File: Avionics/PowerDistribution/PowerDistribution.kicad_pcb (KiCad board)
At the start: 4 copper layers, 90.2 x 96 mm, 165 parts, among them J1 Conn_02x26_Odd_Even, J10 Conn_01x02, J11 Conn_01x04, J12 Conn_01x04, J13 Conn_01x04, J14 Conn_01x02, J15 Conn_01x02, J2 Conn_02x26_Odd_Even, J3 Conn_01x02, J4 Conn_01x02, J5 Conn_01x02, J6 Conn_01x02, J7 USB_C_Receptacle_USB2.0_14P, J8 Conn_01x02, J9 Conn_01x02, Q1 BC848ALT1G, Q2 IRLML2803PBFCT, Q3 IRLML2803PBFCT, U1 LT8610, U16 INA219AxD, U17 INA219AxD, U18 INA219AxD, U19 LT3652EDD, U2 LT8610, U21 INA219AxD, U6 LT8610

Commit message: PDU 3.0.0
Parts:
- added TP1: ~, TestPoint:TestPoint_Pad_2.0x2.0mm, F.Cu at (132.5, 53.5)
- added TP2: ~, TestPoint:TestPoint_Pad_2.0x2.0mm, F.Cu at (132.5, 57.5)
- added TP3: ~, TestPoint:TestPoint_Pad_2.0x2.0mm, F.Cu at (132.5, 61.6)
- added TP4: ~, TestPoint:TestPoint_Pad_2.0x2.0mm, F.Cu at (132.5, 65.6)
- added TP5: ~, TestPoint:TestPoint_Pad_2.0x2.0mm, F.Cu at (136.5, 53.5)
- added TP6: ~, TestPoint:TestPoint_Pad_2.0x2.0mm, F.Cu at (136.5, 57.5)
- added TP7: ~, TestPoint:TestPoint_Pad_2.0x2.0mm, F.Cu at (136.5, 61.6)
- moved C22 62.9 mm to (267.3, 75.2)
- moved U6 62.9 mm to (273.1, 73.7)
- moved C19 62.9 mm to (278.2, 71.9)
- moved C20 62.9 mm to (276.9, 74.9)
- moved C21 62.9 mm to (266.7, 69.1)
- moved C23 62.9 mm to (265.2, 73.4)
- moved C24 62.9 mm to (274.0, 77.9)
- moved L3 62.9 mm to (270.7, 78.4)
- moved R10 62.9 mm to (266.7, 71.1)
- moved R7 62.9 mm to (278.2, 72.9)
- moved R9 62.9 mm to (270.9, 69.3)
- moved R29 53.6 mm to (143.7, 95.3)
- moved C49 53.6 mm to (145.2, 93.8)
- moved C28 53.6 mm to (153.7, 93.8)
- moved R42 53.6 mm to (143.8, 102.1)
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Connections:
- net /BURN_FET renamed BURN_FET
- net /EDFA_5V renamed EDFA_5V
- net /EDFA_5V_STAT renamed EDFA_5V_STAT
- net /ENAB_BURN_1 renamed ENAB_BURN_1
- net /ENAB_BURN_2 renamed ENAB_BURN_2
- net /KAPTON_PWR renamed KAPTON_PWR
- net /SCL renamed SCL
- net /SDA renamed SDA
- net /SOLAR_PRE_INH renamed SOLAR_PRE_INH
- C12 pad 2: /3V3_BUS -> 3V3
- C14 pad 1: /EDFA_5V_SW -> EDFA_5V_S
- C17 pad 1: /5V_BUS -> 5V
- C20 pad 1: GNDA -> V_BATT
- C20 pad 2: V_BATT -> GNDA
- C21 pad 2: /5V_BUS -> 5V
- C24 pad 2: /5V_BUS -> 5V
- C25 pad 1: /5V_BUS -> 5V
- C26 pad 1: /5V_SW_1 -> 5V_S
- C29 pad 1: /3V3_BUS -> 3V3
- C30 pad 1: /PERIPH_PWR -> 3V3_S
- C45 pad 2: /PERIPH_PWR -> 3V3_S
- C46 pad 2: /PERIPH_PWR -> 3V3_S
- C47 pad 2: /PERIPH_PWR -> 3V3_S
- C50 pad 2: /PERIPH_PWR -> 3V3_S
- C9 pad 2: /3V3_BUS -> 3V3
- D1 pad 2: /5V_BUS -> 5V
- D13 pad 2: /PERIPH_PWR -> 3V3_S
- D3 pad 2: /3V3_BUS -> 3V3
- D4 pad 2: /EDFA_5V_SW -> EDFA_5V_S
- D6 pad 2: /5V_SW_1 -> 5V_S
- J1 pad 10: unconnected-(J1-Pin_10-Pad10) -> GND_REF
- J1 pad 11: /KAPTON_ENABLE -> GND_REF
- J1 pad 12: unconnected-(J1-Pin_12-Pad12) -> GND_REF
- J1 pad 13: /EDFA_ENABLE -> /KAPTON_ENABLE
- J1 pad 15: unconnected-(J1-Pin_15-Pad15) -> /EDFA_ENABLE
- J1 pad 9: unconnected-(J1-Pin_9-Pad9) -> GND_REF
- J2 pad 1: /SOLAR_TMP_4 -> unconnected-(J2-Pin_1-Pad1)
- J2 pad 2: /SOLAR_TMP_5 -> /PDU_TEMP
- J2 pad 45: unconnected-(J2-Pin_45-Pad45) -> V_BATT
- L2 pad 2: /3V3_BUS -> 3V3
- L3 pad 2: /5V_BUS -> 5V
- R10 pad 2: /5V_BUS -> 5V
- R57 pad 1: V_BATT -> /BATT_CS
- R58 pad 1: /BATT_CS -> V_BATT
- R58 pad 2: V_BATT -> /BATT_CS
- R59 pad 1: /BATT_CS -> V_BATT
- R8 pad 2: /3V3_BUS -> 3V3
- U10 pad 1: /5V_SW_1 -> 5V_S
- U10 pad 2: /5V_BUS -> 5V
- U10 pad 3: /5V_BUS -> 5V
- U10 pad 4: /5V_SW_1_EN -> 5V_S_EN
- U10 pad 6: /5V_BUS -> 5V
- U10 pad 7: /5V_BUS -> 5V
- U10 pad 8: /5V_SW_1 -> 5V_S
- U14 pad 1: /PERIPH_PWR -> 3V3_S
- U14 pad 2: /3V3_BUS -> 3V3
- U14 pad 3: /3V3_BUS -> 3V3
- U14 pad 4: /PERIPH_EN -> 3V3_S_EN
- U14 pad 6: /3V3_BUS -> 3V3
- U14 pad 7: /3V3_BUS -> 3V3
- U14 pad 8: /PERIPH_PWR -> 3V3_S
- U16 pad 5: /PERIPH_PWR -> 3V3_S
- U17 pad 5: /PERIPH_PWR -> 3V3_S
- U18 pad 5: /PERIPH_PWR -> 3V3_S
- U19 pad 4: /CHRG -> /~{CHRG}
- U19 pad 5: /FAULT -> /~{FAULT}
- U2 pad 14: /3V3_BUS -> 3V3
- U2 pad 15: /3V3_BUS_STAT -> 3V3_STAT
- U21 pad 5: /PERIPH_PWR -> 3V3_S
- U3 pad 1: /EDFA_5V_SW -> EDFA_5V_S
- U3 pad 4: /EDFA_ENABLE -> EDFA_5V_EN
- U3 pad 8: /EDFA_5V_SW -> EDFA_5V_S
- U6 pad 14: /5V_BUS -> 5V
- U6 pad 15: /5V_BUS_STAT -> 5V_STAT
- U9 pad 2: /5V_BUS -> 5V
- U9 pad 3: /5V_BUS -> 5V
- U9 pad 4: /KAPTON_ENABLE -> KAPTON_EN
- U9 pad 6: /5V_BUS -> 5V
- U9 pad 7: /5V_BUS -> 5V
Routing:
- net 3V3_S: track 0.00 -> 124.8 mm, vias 0 -> 5
- net /PERIPH_PWR: track 141.5 -> 16.7 mm, vias 5 -> 0
- net 5V: track 0.00 -> 115.8 mm, vias 0 -> 9
- net /5V_BUS: track 148.9 -> 33.1 mm, vias 9 -> 0
- net (no net): track 0.00 -> 88.5 mm, vias 0 -> 2
- net 5V_S: track 0.00 -> 70.9 mm, vias 0 -> 2
- net /5V_SW_1: track 70.9 -> 0.00 mm, vias 2 -> 0
- net 5V_S_EN: track 0.00 -> 68.1 mm, vias 0 -> 1
- net /5V_SW_1_EN: track 68.1 -> 0.00 mm, vias 1 -> 0
- net EDFA_5V_EN: track 0.00 -> 62.1 mm, vias 0 -> 1
- net /EDFA_ENABLE: track 62.1 -> 0.00 mm, vias 1 -> 0
- net 3V3_S_EN: track 0.00 -> 57.2 mm, vias 0 -> 1
- net /PERIPH_EN: track 57.2 -> 0.00 mm, vias 1 -> 0
- net EDFA_5V_STAT: track 60.9 -> 4.07 mm
- net 3V3: track 0.00 -> 50.9 mm, vias 0 -> 4
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- removed copper zone on B.Cu, net GND
- removed copper zone on F.Cu, net GND
- removed copper zone on In1.Cu, net GND
- removed copper zone on In2.Cu, net V_BATT

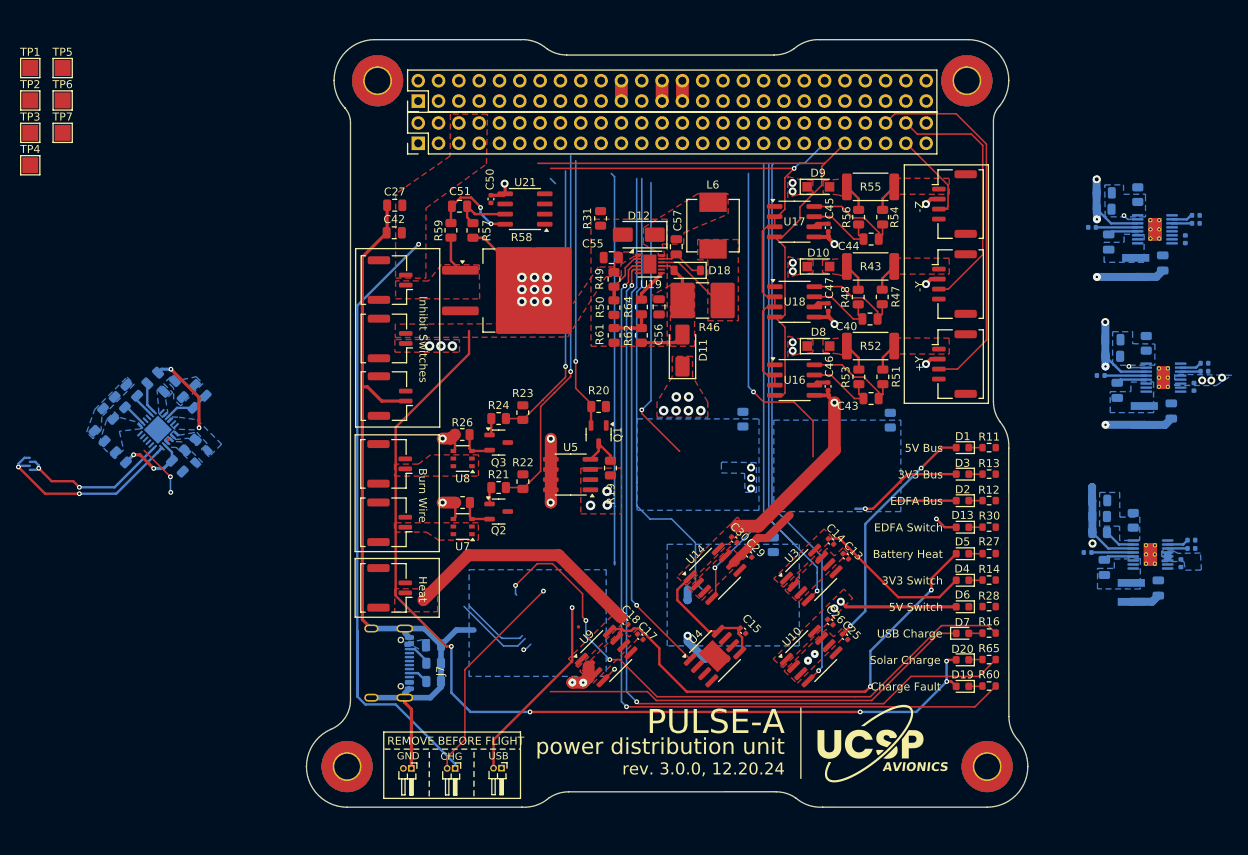
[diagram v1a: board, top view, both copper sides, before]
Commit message: feat: Batt Board v2, PDU v3 in progress; refactor: various cleanups
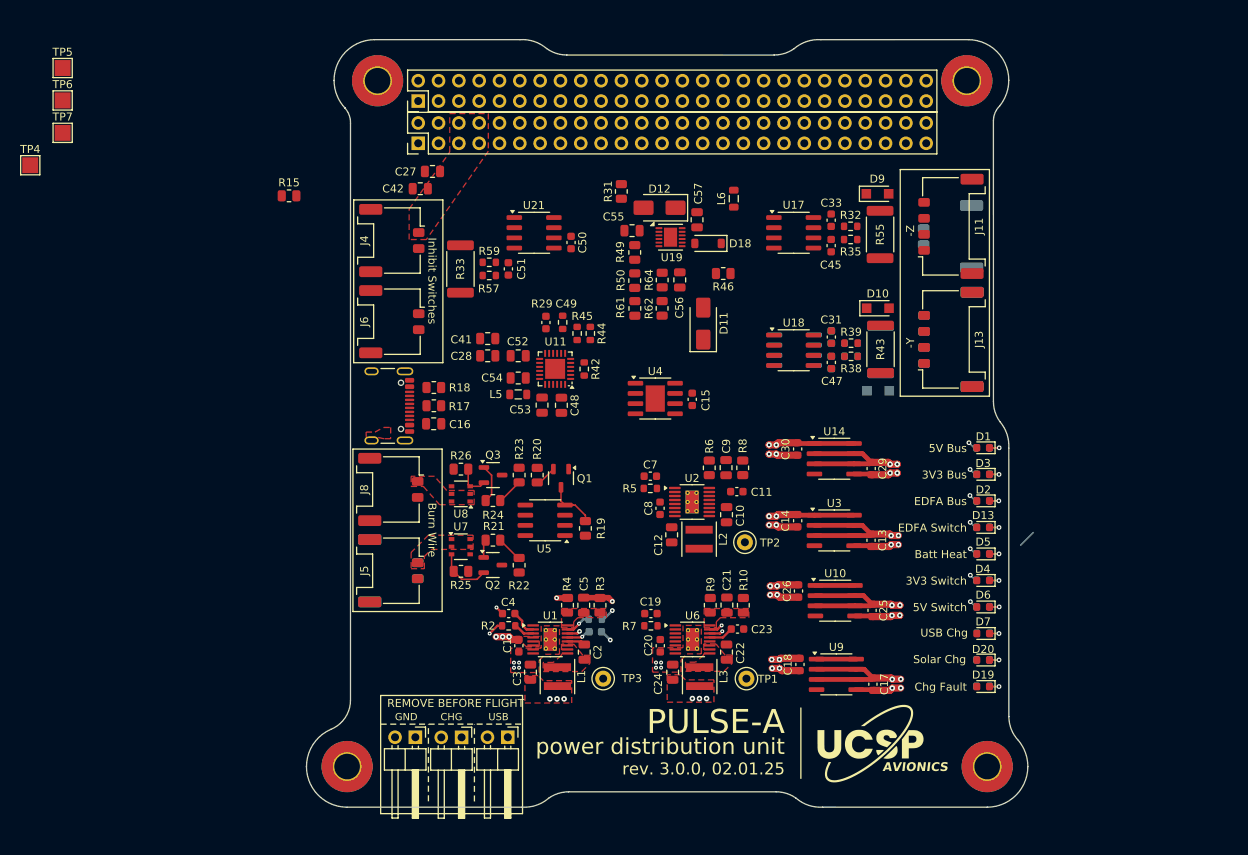
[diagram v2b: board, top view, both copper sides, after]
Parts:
- removed C40, C43, C44: 1uF, Capacitor_SMD:C_0805_2012Metric
- removed R34: 0, Resistor_SMD:R_0805_2012Metric
- removed R47, R48, R51, R53, R54, R56: 10, Resistor_SMD:R_0805_2012Metric
- removed R58: 2m, Package_TO_SOT_SMD:TO-263-2
- added C31: 1uF, Capacitor_SMD:C_0603_1608Metric, F.Cu at (232.6, 87.1)
- added C32: 1uF, Capacitor_SMD:C_0603_1608Metric, B.Cu at (232.6, 90.3)
- added C33: 1uF, Capacitor_SMD:C_0603_1608Metric, F.Cu at (232.6, 72.5)
- added R32: 10, Resistor_SMD:R_0603_1608Metric, F.Cu at (235.0, 73.3)
- added R35: 10, Resistor_SMD:R_0603_1608Metric, F.Cu at (235.0, 74.9)
- added R36: 10, Resistor_SMD:R_0603_1608Metric, B.Cu at (235.1, 87.9)
- added R37: 10, Resistor_SMD:R_0603_1608Metric, B.Cu at (235.1, 89.5)
- added R38: 10, Resistor_SMD:R_0603_1608Metric, F.Cu at (235.1, 89.5)
- added R39: 10, Resistor_SMD:R_0603_1608Metric, F.Cu at (235.1, 87.9)
- C1, C11, C19, C20, C23, C4, C7, C8: footprint Capacitor_SMD:C_0402_1005Metric -> Capacitor_SMD:C_0603_1608Metric; moved to F.Cu
- C10, C12, C16, C2, C21, C22, C24, C28, C3, C41, C48, C5, C52, C53, C54, C9, J7, L1, L2, L3, L5, R10, R15, R17, R18, R3, R4, R6, R8, R9, U1, U11, U2, U6: moved to F.Cu
- C13, C14, C15, C17, C18, C25, C26, C29, C30, C45, C47, C50, C6: footprint Capacitor_SMD:C_0402_1005Metric -> Capacitor_SMD:C_0603_1608Metric
- C46: footprint Capacitor_SMD:C_0402_1005Metric -> Capacitor_SMD:C_0603_1608Metric; moved to B.Cu
- C49: footprint Capacitor_SMD:C_0805_2012Metric -> Capacitor_SMD:C_0603_1608Metric; moved to F.Cu
- C51: footprint Capacitor_SMD:C_0805_2012Metric -> Capacitor_SMD:C_0603_1608Metric
- D13, D4, D5, D6: value 150060RS75000 -> 150060AS75000
- D8, R11, R12, R13, R14, R16, R27, R28, R52, R60, R65, U16: moved to B.Cu
- J10, J14, J9: footprint Connector_PinHeader_1.00mm:PinHeader_1x02_P1.00mm_Horizontal -> Connector_PinHeader_2.54mm:PinHeader_1x02_P2.54mm_Horizontal
- J11, J13: footprint Connector_Molex:Molex_CLIK-Mate_502382-0470_1x04-1MP_P1.25mm_Vertical -> Connector_Molex:Molex_Pico-Lock_205338-0004_1x04-1MP_P2.00mm_Horizontal
- J12: footprint Connector_Molex:Molex_CLIK-Mate_502382-0470_1x04-1MP_P1.25mm_Vertical -> Connector_Molex:Molex_Pico-Lock_205338-0004_1x04-1MP_P2.00mm_Horizontal; moved to B.Cu
- J15, J3: footprint Connector_Molex:Molex_CLIK-Mate_502382-0270_1x02-1MP_P1.25mm_Vertical -> Connector_Molex:Molex_Pico-Lock_205338-0002_1x02-1MP_P2.00mm_Horizontal; moved to B.Cu
- J4, J5, J6, J8: footprint Connector_Molex:Molex_CLIK-Mate_502382-0270_1x02-1MP_P1.25mm_Vertical -> Connector_Molex:Molex_Pico-Lock_205338-0002_1x02-1MP_P2.00mm_Horizontal
- L6: footprint Inductor_SMD:L_Vishay_IHLP-2525 -> Inductor_SMD:L_0805_2012Metric
- R1, R57, R59: footprint Resistor_SMD:R_0805_2012Metric -> Resistor_SMD:R_0603_1608Metric
- R2, R5, R7: footprint Capacitor_SMD:C_0402_1005Metric -> Resistor_SMD:R_0603_1608Metric; moved to F.Cu
- R29, R42, R44, R45: footprint Resistor_SMD:R_0805_2012Metric -> Resistor_SMD:R_0603_1608Metric; moved to F.Cu
- R30: value 150 -> 65; moved to B.Cu
- R33: value 0 -> 2m; footprint Resistor_SMD:R_0805_2012Metric -> Resistor_SMD:R_2512_6332Metric; moved to F.Cu
- R46: footprint Resistor_SMD:R_2816_7142Metric -> Resistor_SMD:R_0805_2012Metric
- TP1, TP2, TP3: footprint TestPoint:TestPoint_Pad_2.0x2.0mm -> TestPoint:TestPoint_Keystone_5000-5004_Miniature
- moved TP1 117.6 mm to (222.0, 129.8)
- moved TP2 105.0 mm to (221.8, 112.8)
- moved TP3 98.9 mm to (204.1, 129.8)
- moved R2 85.9 mm to (192.3, 123.2), turned to 180 degrees
- moved C4 85.8 mm to (192.3, 121.7), turned to 0 degrees
- moved R7 84.7 mm to (210.1, 123.2), turned to 180 degrees
- moved C19 84.4 mm to (210.1, 121.7), turned to 0 degrees
- moved C1 83.4 mm to (193.5, 125.7)
- moved C20 83.0 mm to (211.2, 125.7), turned to -90 degrees
- moved C24 79.8 mm to (212.8, 129.0)
- moved C3 79.2 mm to (195.0, 129.0)
- moved U6 77.2 mm to (215.3, 124.9), turned to 0 degrees
- moved U1 75.8 mm to (197.5, 124.9), turned to 0 degrees
- moved L3 74.7 mm to (216.2, 129.6)
- moved R15 74.6 mm to (164.8, 69.5), turned to 0 degrees
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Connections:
- net /EDFA_ENABLE renamed /EDFA_EN
- C1 pad 1: GNDA -> GND
- C11 pad 2: GNDA -> GND
- C12 pad 1: GNDA -> GND
- C15 pad 2: /PERIPH_PWR -> 3V3
- C19 pad 1: GNDA -> GND
- C20 pad 2: GNDA -> GND
- C23 pad 2: GNDA -> GND
- C24 pad 1: GNDA -> GND
- C27 pad 2: /BATT_PRE_INH -> /BATT_RAW
- C3 pad 1: GNDA -> GND
- C4 pad 1: GNDA -> GND
- C42 pad 2: /BATT_PRE_INH -> /BATT_RAW
- C6 pad 2: GNDA -> GND
- C7 pad 1: GNDA -> GND
- C8 pad 1: GNDA -> GND
- J1 pad 13: /KAPTON_ENABLE -> KAPTON_EN
- J1 pad 21: /5V_SW_1 -> 5V_S
- J1 pad 22: /ICL -> /FAULT
- J1 pad 31: /5V_SW_1_EN -> 5V_S_EN
- J1 pad 5: /BATT_PRE_INH -> /RAW_BATT
- J1 pad 6: /BATT_PRE_INH -> /RAW_BATT
- J1 pad 7: /BATT_PRE_INH -> /RAW_BATT
- J1 pad 8: /BATT_PRE_INH -> /RAW_BATT
- J2 pad 21: /EDFA_5V_SW -> EDFA_5V_S
- J2 pad 22: /EDFA_5V_SW -> EDFA_5V_S
- J2 pad 25: /5V_BUS -> 5V
- J2 pad 26: /5V_BUS -> 5V
- J2 pad 27: /3V3_BUS -> 3V3
- J2 pad 28: /3V3_BUS -> 3V3
- J4 pad 1: /BATT_CS -> /BATT_RAW
- J4 pad 2: /BATT_PRE_INH -> /BATT_CS
- J9 pad 1: /BATT_PRE_INH -> /BATT_RAW
- R2 pad 2: GNDA -> GND
- R33 pad 1: GNDA -> /BATT_CS
- R33 pad 2: GND -> V_BATT
- R4 pad 1: GNDA -> GND
- R5 pad 2: GNDA -> GND
- R6 pad 1: GNDA -> GND
- R7 pad 2: GNDA -> GND
- R9 pad 1: GNDA -> GND
- U1 pad 17: GNDA -> GND
- U1 pad 7: GNDA -> GND
- U1 pad 8: GNDA -> GND
- U19 pad 3: unconnected-(U19-~{SHDN}-Pad3) -> /SHDN
- U2 pad 17: GNDA -> GND
- U2 pad 7: GNDA -> GND
- U2 pad 8: GNDA -> GND
- U4 pad 5: /PERIPH_PWR -> 3V3
- U4 pad 8: /PERIPH_PWR -> 3V3
- U6 pad 17: GNDA -> GND
- U6 pad 7: GNDA -> GND
- U6 pad 8: GNDA -> GND
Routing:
- net /SOLAR_PRE_MPPT: track 122.0 -> 0.00 mm, vias 5 -> 0
- net 3V3_S: track 124.8 -> 10.8 mm, vias 5 -> 2
- net /CHRG: track 103.9 -> 0.00 mm, vias 2 -> 0
- net /FAULT: track 102.8 -> 0.00 mm, vias 2 -> 0
- net GND_REF: track 101.7 -> 0.00 mm
- net (no net): track 88.5 -> 0.00 mm, vias 2 -> 0
- net /BATT_PRE_INH: track 84.3 -> 0.00 mm, vias 1 -> 0
- net KAPTON_PWR: track 89.0 -> 8.54 mm
- net /REGN: track 79.3 -> 0.00 mm, vias 3 -> 0
- net 5V: track 115.8 -> 38.0 mm, vias 9 -> 8
- net SCL: track 75.2 -> 0.00 mm
- net 5V_S_EN: track 68.1 -> 0.00 mm, vias 1 -> 0
- net SDA: track 64.8 -> 0.00 mm, vias 1 -> 0
- net /PDU_TEMP: track 63.4 -> 0.00 mm, vias 1 -> 0
- net 5V_S: track 70.9 -> 8.55 mm
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- added copper zone on F.Cu, net /BATT_RAW
- added copper zone on F.Cu, net /FB_1
- added copper zone on F.Cu, net /FB_3
- added copper zone on F.Cu, net /SW_1
- added copper zone on F.Cu, net /SW_3
- added copper zone on F.Cu, net /V_BUS
- added copper zone on In2.Cu, net 3V3
- added copper zone on In2.Cu, net 3V3_S
- added copper zone on F.Cu, net 5V
- added copper zone on In2.Cu, net 5V
- added copper zone on In2.Cu, net 5V_S
- added copper zone on In2.Cu, net EDFA_5V
- added copper zone on In2.Cu, net EDFA_5V_S
- added copper zone on F.Cu, net GND
- added copper zone on In1.Cu, net GND
- added copper zone on In2.Cu, net KAPTON_PWR
- added copper zone on In2.Cu, net V_BATT
- removed copper zone on F.Cu, net /3V3_BUS
- removed copper zone on F.Cu, net /5V_BUS
- removed copper zone on F.Cu, net /5V_SW_1
- removed copper zone on F.Cu, net /BATT_CS
- removed copper zone on F.Cu, net /BATT_PRE_INH
- removed copper zone on B.Cu, net /CHRG_RBF
- removed copper zone on F.Cu, net /EDFA_5V_SW
- removed copper zone on B.Cu, net /FB_1
- removed copper zone on B.Cu, net /FB_2
- removed copper zone on B.Cu, net /FB_3
- removed copper zone on F.Cu, net /OUT
- removed copper zone on F.Cu, net /PERIPH_PWR
- removed copper zone on B.Cu, net /PMID
- removed copper zone on F.Cu, net /SENSE
- removed copper zone on F.Cu, net /SOLAR_IN_+Y
- removed copper zone on F.Cu, net /SOLAR_IN_-Y
- removed copper zone on F.Cu, net /SOLAR_IN_-Z
- removed copper zone on F.Cu, net /SOLAR_PRE_MPPT
- removed copper zone on B.Cu, net /SW
- removed copper zone on B.Cu, net /SW_1
- removed copper zone on B.Cu, net /SW_2
- removed copper zone on B.Cu, net /SW_3
- removed copper zone on F.Cu, net /SW_CHRG
- removed copper zone on B.Cu, net /THM
- removed copper zone on B.Cu, net /V_BUS
- removed copper zone on F.Cu, net /sol_1_diode
- removed copper zone on F.Cu, net /sol_2_diode
- removed copper zone on F.Cu, net /sol_3_diode
- removed copper zone on B.Cu, net GNDA
- removed copper zone on F.Cu, net GNDA
- removed copper zone on B.Cu, net GND_REF
- removed copper zone on F.Cu, net KAPTON_PWR
- removed copper zone on F.Cu, net SOLAR_PRE_INH
- removed copper zone on In1.Cu, net SOLAR_PRE_INH
- removed copper zone on B.Cu, net V_BATT
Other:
- board text added: "Batt Heat"
- board text added: "Chg Fault"
- board text added: "Solar Chg"
- board text added: "USB Chg"
- board text added: "rev. 3.0.0, 02.01.25"
- board text removed: "Battery Heat"
- board text removed: "Charge Fault"
- board text removed: "Solar Charge"
- board text removed: "USB Charge"
- board text removed: "rev. 3.0.0, 12.20.24"
